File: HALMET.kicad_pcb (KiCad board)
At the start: 4 copper layers, 89 x 58 mm, 242 parts, among them J1103 Conn_01x02, J1104 Conn_01x02, J1105 Conn_01x02, J1106 Conn_01x02, J1201 Conn_01x02, J201 GPIO, J203 Conn_01x01, J302 Conn_01x02, J401 USB_B_Micro, J501 EXT LEDS, J602 Conn_02x04_Odd_Even, J604 Conn_01x02, J605 Conn_01x02, J606 Conn_01x02, J607 Conn_01x02, J702 Conn_01x04, J801 Conn_01x03, J802 Conn_01x04, Q401 S8050, Q402 S8050, Q601 BC856BW,115, Q602 BC856BW,115, Q603 BC856BW,115, Q604 BC856BW,115, SW501 SW_Push, SW502 SW_Push, U1101 74LVC1G17, U1102 74LVC1G17, U1103 74LVC1G17, U1104 74LVC1G17, U1200 ICM-42688-P, U1201 π140U30, U1202 ISO1540, U1203 XC6206P332MR, U201 ESP32-WROOM-32UE-N16, U202 XL1509-3.3, U203 LM317L_SOT-89, U401 CH340C, U501 SN65HVD230DR, U601 LMV324, U602 ADS1115IDGS

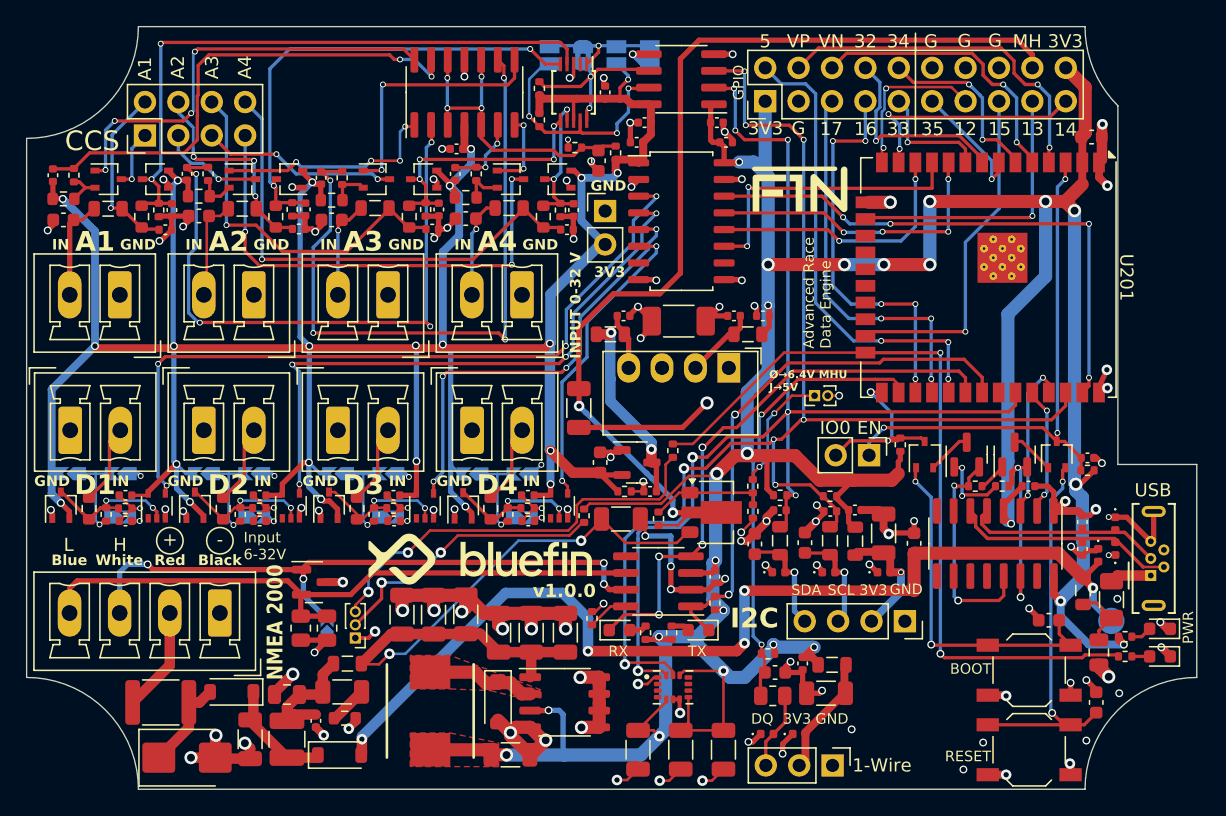
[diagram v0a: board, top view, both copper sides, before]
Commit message: Added RS485/RS233 (NMEA 01830) chip
Added SP3485EN RS485 bi-directional driver with a GPIO toggle for changing input - output direction.

Connected to GPIO pin header
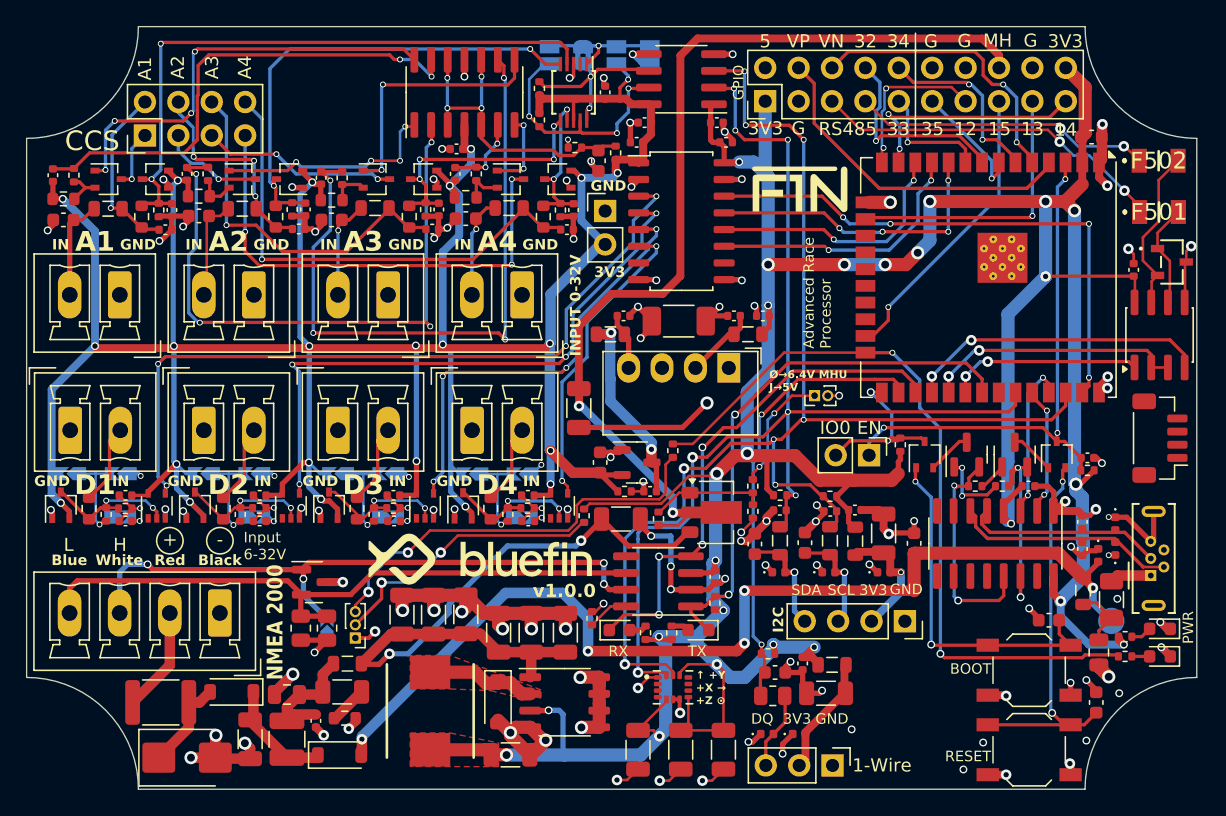
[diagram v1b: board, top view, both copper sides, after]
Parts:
- added C616: 100nF, Capacitor_SMD:C_0402_1005Metric, F.Cu at (173.2, 75.5)
- added CR501: PSM712-LF-T7, PSM712-LF-T7:CR_SOT-23_PTD, F.Cu at (176.1, 74.9)
- added F501: 1206L010/60WR, 1206L010_60WR:1206L075132WR, F.Cu at (175.1, 71.1)
- added F502: 1206L010/60WR, 1206L010_60WR:1206L075132WR, F.Cu at (175.1, 67.2)
- added REF**: JST_SH_BM04B-SRSS-TB_1x04-1MP_P1.00mm_Vertical, Connector_JST:JST_SH_BM04B-SRSS-TB_1x04-1MP_P1.00mm_Vertical, F.Cu at (175.2, 88.3)
- added U502: SP3485EN, Package_SO:SOIC-8_3.9x4.9mm_P1.27mm, F.Cu at (175.2, 80.5)
- U201: value ESP32-WROOM-32UE-N16 -> ESP32-WROOM-32UE-N16R2
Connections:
- J201 pad 16: GND -> /MHU_VSUP
- J201 pad 18: /MHU_VSUP -> GND
- J201 pad 2: /ESP32/IO5 -> GND
- J201 pad 5: /ESP32/IO17 -> /RS485_1_A
- J201 pad 7: /ESP32/IO16 -> /RS485_1_B
- U201 pad 27: /ESP32/IO16 -> /CAN_RX
- U201 pad 28: /ESP32/IO17 -> /UART1_TX
- U201 pad 29: /ESP32/IO5 -> /I-O_RS485
- U201 pad 30: /CAN_RX -> /UART1_RX
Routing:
- net /ESP32/IO5: track 35.7 -> 0.00 mm, vias 3 -> 0
- net /ESP32/IO16: track 30.1 -> 0.00 mm, vias 5 -> 0
- net /ESP32/IO17: track 28.7 -> 0.00 mm, vias 3 -> 0
- net /RS485_1_A: track 0.00 -> 27.2 mm, vias 0 -> 2
- net /UART1_TX: track 0.00 -> 23.7 mm, vias 0 -> 2
- net /RS485_1_B: track 0.00 -> 22.7 mm, vias 0 -> 2
- net /I-O_RS485: track 0.00 -> 20.9 mm, vias 0 -> 2
- net /UART1_RX: track 0.00 -> 14.7 mm, vias 0 -> 2
- net Net-(U502-B): track 0.00 -> 12.6 mm
- net +3.3V: track 274.8 -> 283.1 mm, vias 24 -> 25
- net Net-(U502-A): track 0.00 -> 8.04 mm
- net GND: track 155.6 -> 160.6 mm, vias 76 -> 78
- net /CAN_RX: track 43.5 -> 39.4 mm
- net /ESP32/TDO: track 26.3 -> 22.4 mm
- net /LED: track 60.1 -> 57.9 mm
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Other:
- outline, holes or cut-outs redrawn
- board text added: "Advanced Race Processor"
- board text added: "INPUT 0-32V"
- board text added: "RS485"
- board text added: "↑ +Y +X → +Z ⊙"
- board text removed: "16"
- board text removed: "17"
- board text removed: "Advanced Race Data Engine"
- board text removed: "INPUT 0-32 V"

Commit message: Changed to ESP32-S3-WROOM-1U
Added ESP32-S3-WROOM-1U-N16R2  and updated all routing and pin assignments.

Added USB-OTG connected via JST-PH
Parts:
- removed the REF** at (175.2, 88.3)
- added J402: Conn_01x04, Connector_JST:JST_SH_BM04B-SRSS-TB_1x04-1MP_P1.00mm_Vertical, F.Cu at (175.0, 88.6)
- U201: value ESP32-WROOM-32UE-N16R2 -> ESP32-S3-WROOM-1U-N16R2; footprint RF_Module:ESP32-WROOM-32UE -> RF_Module:ESP32-S3-WROOM-1U
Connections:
- net /ESP32/SENSOR_VN renamed /ESP32/IO5
- net /ESP32/SENSOR_VP renamed /ESP32/IO4
- J201 pad 10: /ESP32/IO34 -> /ESP32/IO38
- J201 pad 11: /ESP32/IO35 -> /ESP32/TDO
- J201 pad 15: /ESP32/TDO -> /ESP32/TMS
- J201 pad 17: /ESP32/TCK -> /ESP32/IO15
- J201 pad 19: /ESP32/TMS -> /ESP32/IO7
- J201 pad 8: /ESP32/IO32 -> /ESP32/IO48
- J201 pad 9: /ESP32/IO33 -> /ESP32/TCK
- U201 pad 10: /DI2 -> /RS485_RX
- U201 pad 11: /DI4 -> /RS485_TX
- U201 pad 12: /DI3 -> unconnected-(U201-IO8-Pad12)
- U201 pad 13: /ESP32/TMS -> /USB_D_MINUS
- U201 pad 14: /ESP32/TDI -> /USB_D_PLUS
- U201 pad 15: GND -> unconnected-(U201-IO3-Pad15)
- U201 pad 16: /ESP32/TCK -> unconnected-(U201-IO46-Pad16)
- U201 pad 17: unconnected-(U201-SHD/SD2-Pad17) -> /DI1
- U201 pad 18: unconnected-(U201-SWP/SD3-Pad18) -> /DI2
- U201 pad 19: unconnected-(U201-SCS/CMD-Pad19) -> /DI3
- U201 pad 20: unconnected-(U201-SCK/CLK-Pad20) -> /DI4
- U201 pad 21: unconnected-(U201-SDO/SD0-Pad21) -> /LED
- U201 pad 22: unconnected-(U201-SDI/SD1-Pad22) -> /CAN_TX
- U201 pad 23: /ESP32/TDO -> /CAN_RX
- U201 pad 24: /LED -> /DQ
- U201 pad 25: /ESP32/IO0 -> /ESP32/IO48
- U201 pad 26: /DQ -> unconnected-(U201-IO45-Pad26)
- U201 pad 27: /CAN_RX -> /ESP32/IO0
- U201 pad 28: /UART1_TX -> unconnected-(U201-IO35-Pad28)
- U201 pad 29: /I-O_RS485 -> unconnected-(U201-IO36-Pad29)
- U201 pad 30: /UART1_RX -> unconnected-(U201-IO37-Pad30)
- U201 pad 31: /CAN_TX -> /ESP32/IO38
- U201 pad 32: unconnected-(U201-NC-Pad32) -> /ESP32/TCK
- U201 pad 33: /SDA -> /ESP32/TDO
- U201 pad 34: /USB_TXD -> /ESP32/TDI
- U201 pad 35: /USB_RXD -> /ESP32/TMS
- U201 pad 36: /SCL -> /USB_UART_TXD
- U201 pad 37: /DI1 -> /USB_UART_RXD
- U201 pad 38: GND -> /SDA
- U201 pad 39: GND -> /SCL
- U201 pad 6: /ESP32/IO34 -> /I-O_RS485
- U201 pad 7: /ESP32/IO35 -> /ESP32/IO7
- U201 pad 8: /ESP32/IO32 -> /ESP32/IO15
- U201 pad 9: /ESP32/IO33 -> unconnected-(U201-IO16-Pad9)
- U401 pad 2: /USB_TXD -> /USB_UART_TXD
- U401 pad 3: /USB_RXD -> /USB_UART_RXD
- U502 pad 1: /UART1_RX -> /RS485_TX
- U502 pad 4: /UART1_TX -> /RS485_RX
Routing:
- net /USB_D_PLUS: track 0.00 -> 33.2 mm
- net /USB_D_MINUS: track 0.00 -> 31.8 mm
- net /DI1: track 41.7 -> 11.5 mm, vias 4 -> 0
- net /ESP32/IO48: track 0.00 -> 27.4 mm, vias 0 -> 2
- net /ESP32/IO38: track 0.00 -> 27.1 mm, vias 0 -> 2
- net /RS485_RX: track 0.00 -> 26.2 mm, vias 0 -> 2
- net /RS485_TX: track 0.00 -> 23.7 mm, vias 0 -> 2
- net /UART1_TX: track 23.7 -> 0.00 mm, vias 2 -> 0
- net /ESP32/IO32: track 15.1 -> 0.00 mm, vias 1 -> 0
- net /UART1_RX: track 14.7 -> 0.00 mm, vias 2 -> 0
- net /ESP32/IO34: track 13.7 -> 0.00 mm, vias 2 -> 0
- net /USB_RXD: track 11.5 -> 0.00 mm, vias 2 -> 0
- net /USB_UART_RXD: track 0.00 -> 11.5 mm, vias 0 -> 2
- net /ESP32/TDI: track 12.4 -> 23.8 mm
- net /DI2: track 22.9 -> 12.1 mm, vias 4 -> 0
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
